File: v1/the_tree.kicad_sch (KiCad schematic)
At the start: 102 parts, among them SW48 Q

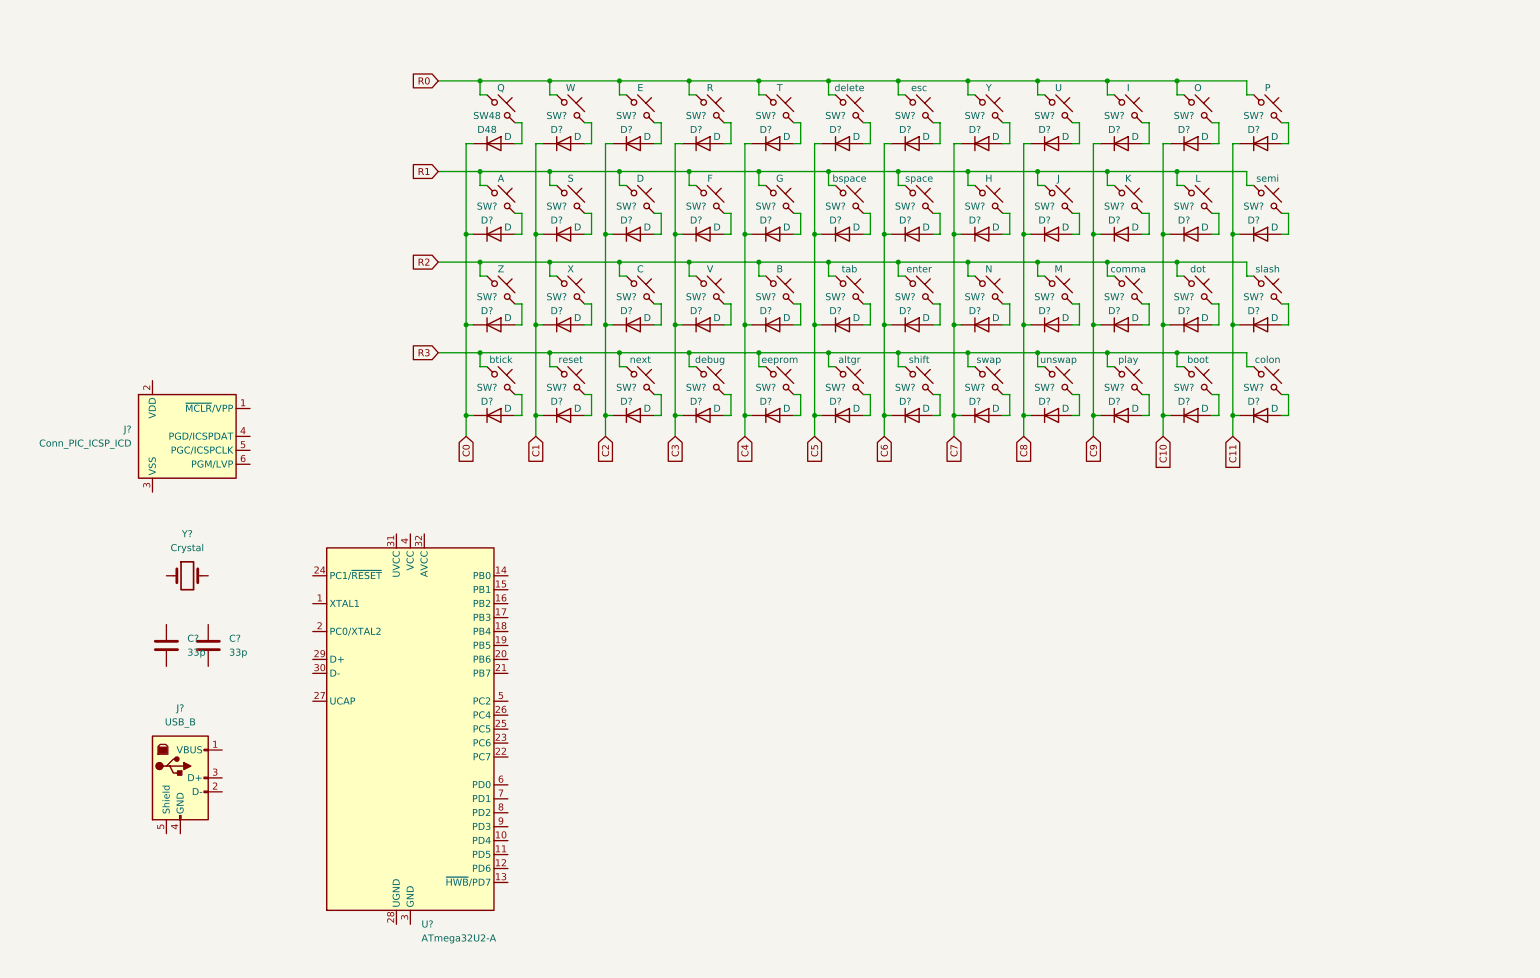
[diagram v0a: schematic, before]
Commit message: schematic and footprints from ai03
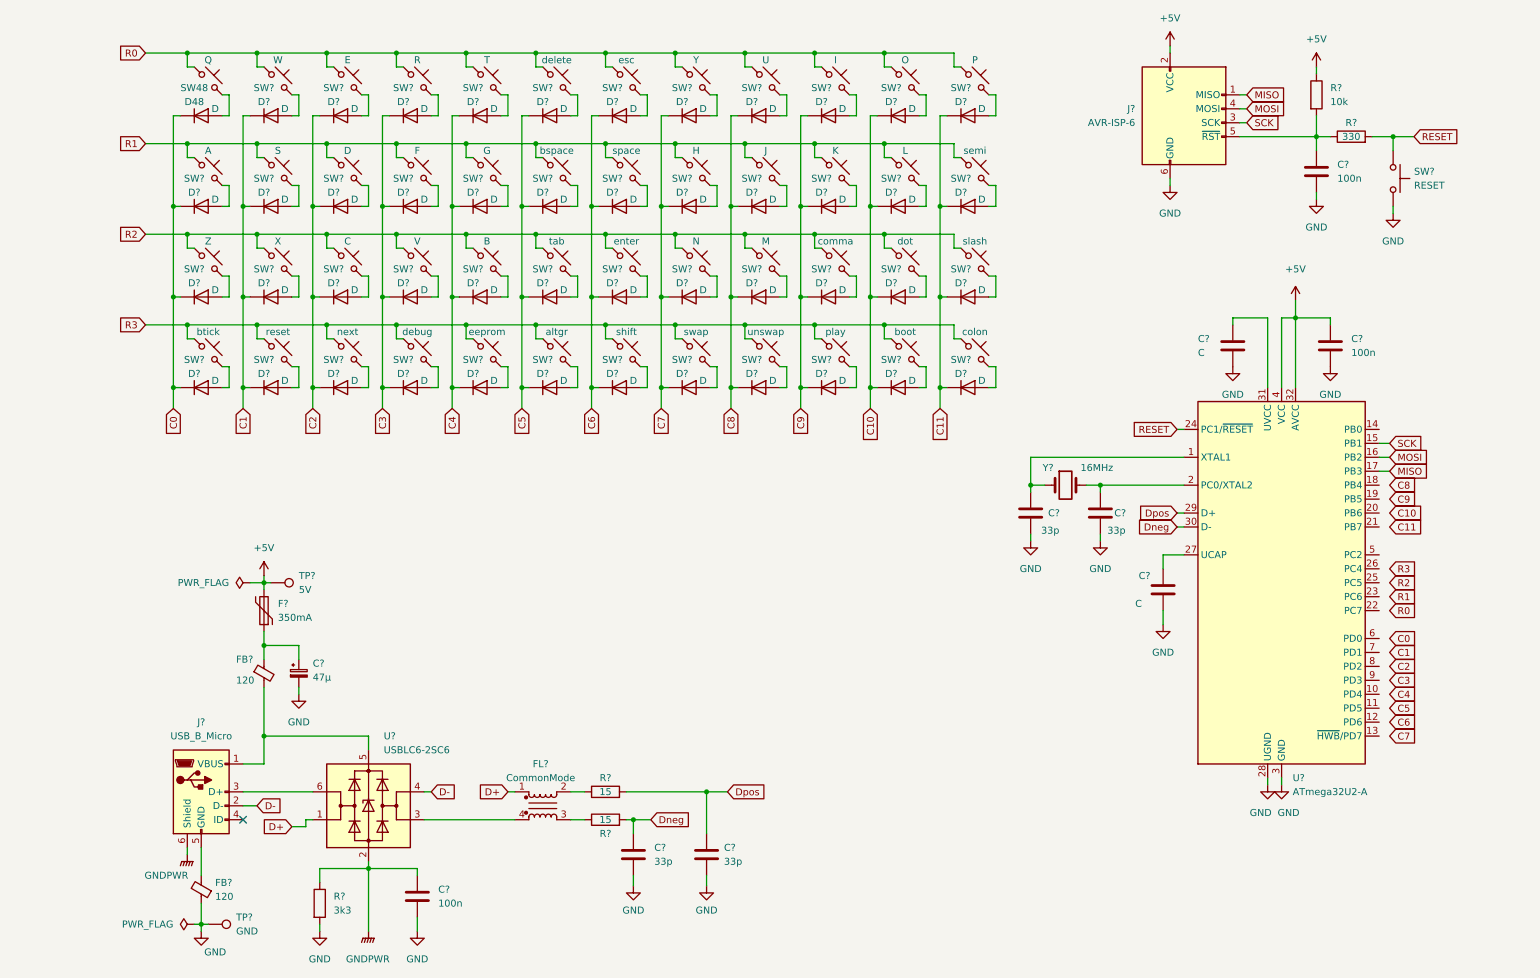
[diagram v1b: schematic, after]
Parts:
- removed J?: Conn_PIC_ICSP_ICD, symbol Connector:Conn_PIC_ICSP_ICD
- removed J?: USB_B, symbol Connector:USB_B
- added C? (x3): 100n, symbol Device:C
- added C? (x2): 33p, symbol Device:C
- added C? (x2): C, symbol Device:C
- added C?: 47µ, symbol Device:C_Polarized_Small
- added F?: 350mA, symbol Device:Polyfuse
- added FB? (x2): 120, symbol Device:FerriteBead_Small
- added FL?: CommonMode, symbol the_tree:Filter_EMI_CommonMode
- added J?: AVR-ISP-6, symbol Connector:AVR-ISP-6
- added J?: USB_B_Micro, symbol Connector:USB_B_Micro
- added R?: 3k3, symbol Device:R
- added R?: 330, symbol Device:R
- added R? (x2): 15, symbol Device:R
- added R?: 10k, symbol Device:R
- added SW?: RESET, symbol Switch:SW_Push
- added TP?: 5V, symbol Connector:TestPoint
- added TP?: GND, symbol Connector:TestPoint
- added U?: USBLC6-2SC6, Package_TO_SOT_SMD:SOT-23-6, symbol Power_Protection:USBLC6-2SC6
- Y?: value Crystal -> 16MHz
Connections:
- net at U?.1 (XTAL1): now also C?.1, Y?.1
- net SCK: now reaches U?.15 (PB1)
- net SCK: now also J?.3 (SCK)
- net MOSI: now reaches U?.16 (PB2)
- net MOSI: now also J?.4 (MOSI)
- net MISO: now reaches U?.17 (PB3)
- net MISO: now also J?.1 (MISO)
- net at U?.2 (PC0/XTAL2): now also C?.1, Y?.2
- net RESET: now reaches U?.24 (PC1/~{RESET})
- net RESET: now also R?.2, SW?.1
- net at U?.27 (UCAP): now also C?.1
- net GND: now reaches U?.28 (UGND)
- net GND: now also C?.2, C?.2, U?.3 (GND), C?.2, C?.2, C?.2, C?.2, C?.2, C?.2, C?.2, C?.2, FB?.1, J?.6 (GND), R?.2, SW?.2, TP?.1
- net Dpos: now reaches U?.29 (D+)
- net Dpos: now also C?.1, R?.2
- net Dneg: now reaches U?.30 (D-)
- net Dneg: now also C?.1, R?.2
- net at U?.31 (UVCC): now also C?.1
- net +5V: now reaches U?.32 (AVCC)
- net +5V: now also U?.4 (VCC), C?.1, F?.2, J?.2 (VCC), R?.1, TP?.1
- new net: C?.1, J?.5 (~{RST}), R?.1, R?.2
- new net: C?.1, F?.1, FB?.1
- new net: FB?.2, J?.5 (GND)
- new net: FL?.3, R?.1
- new net: FL?.2, R?.1
- new net: FL?.4, U?.3 (I/O2)
- new net: FB?.2, J?.1 (VBUS), U?.5 (VBUS)
- new net: J?.3 (D+), U?.6 (I/O1)
- new net D+: FL?.1, U?.1 (I/O1)
- new net D-: J?.2 (D-), U?.4 (I/O2)
- new net GNDPWR: C?.1, J?.6 (Shield), R?.1, U?.2 (GND)
- no-connect marks 0 -> 1
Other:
- moved on the sheet: C?, D48, D?, SW48, SW?, U?, Y?

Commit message: Schematic for full keyboard
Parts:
- removed C? (x2): 33p, symbol Device:C
- removed C?: 47µ, symbol Device:C_Polarized_Small
- removed D? (x4): D, symbol Device:D
- added C1: 4µ7, symbol Device:C
- added D44: LED, symbol Device:LED
- added H1: case, symbol Mechanical:MountingHole_Pad
- added R6: 10k, symbol Device:R
- added R7: 1k, symbol Device:R
- added SW50: BOOT, symbol Switch:SW_Push
- C5, C6: renamed from C?; value C -> 1µ
- C8: renamed from C?; value 100n -> 1µ
- R2, R3: renamed from R?; value 15 -> 22
- R5: renamed from R?; value 330 -> 22
- gave numbers to parts that had none: 108
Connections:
- net +5V: now also C6.1, U2.31 (UVCC), R6.1
- net C0: now also U2.6 (PD0)
- net C1: now also U2.7 (PD1)
- net C10: now also U2.20 (PB6)
- net C11: now also U2.21 (PB7)
- net C2: now also U2.8 (PD2)
- net C3: now also SW15.2, U2.9 (PD3)
- net C4: now also SW19.2, U2.10 (PD4)
- net C5: now also U2.11 (PD5)
- net C6: now also U2.12 (PD6)
- net C7: now also SW31.2, U2.14 (PB0)
- net C8: now also SW35.2, U2.18 (PB4)
- net C9: now also U2.19 (PB5)
- net GND: now also J1.4 (ID), C1.2, D44.1 (K), SW50.2
- net GNDPWR: now also H1.1
- net R0: now also U2.22 (PC7)
- net R1: now also U2.23 (PC6)
- net R2: now also U2.25 (PC5)
- net R3: now also U2.26 (PC4)
- net at U2.13 (~{HWB}/PD7): now also R6.2, SW50.1
- net at U2.5 (PC2): now also R7.1
- net at F1.1, FB2.1: now also C1.1
- net RESET renamed ~{RESET}
- new net: D44.2 (A), R7.2
- no-connect marks 1 -> 0
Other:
- moved on the sheet: C2, C3, C4, C5, C6, C7, C8, D1, D10, D11, D12, D13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

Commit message: Earth connection on the other side of filter
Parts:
- removed SW50: BOOT, symbol Switch:SW_Push
- C3, C4: value 33p -> 22p
- R1: value 3k3 -> 10k
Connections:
- net +5V: no longer R6.1
- net GND: now also R6.2; no longer R1.2
- net GNDPWR: now also R1.2; no longer R1.1
- net at U2.13 (~{HWB}/PD7): now also R6.1; no longer R6.2
- net at FB1.2, J1.5 (GND): now also R1.1
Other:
- moved on the sheet: C1, C2, C7, F1, FB1, FB2, FL1, H1, J1, J2, R1, R2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

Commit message: 40 keys
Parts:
- R1: value 10k -> 1M
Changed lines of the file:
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@@
     (in_bom yes) (on_board yes)
     (property "Reference" "R1" (id 0) (at 139.065 151.13 90))
-    (property "Value" "10k" (id 1) (at 139.065 153.67 90))
+    (property "Value" "1M" (id 1) (at 139.065 153.67 90))
     (property "Footprint" "" (id 2) (at 139.065 155.448 90)
       (effects (font (size 1.27 1.27)) hide)
@@
     )
     (path "/22c6e9fd-8440-4742-b3a7-0af3a4452d93"
-      (reference "R1") (unit 1) (value "10k") (footprint "")
+      (reference "R1") (unit 1) (value "1M") (footprint "")
     )
     (path "/dccaf421-4b06-4a6c-9285-c0b383a533f7"
